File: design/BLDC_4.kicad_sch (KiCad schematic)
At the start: 39 parts, among them J1 Conn_01x03, J2 Conn_01x02, J3 Conn_02x06_Odd_Even, J6 Conn_02x06_Odd_Even, K1 SERVO, P101 CANBUS, P3 PWR_COMM, U8 MAX485ED, X1 MINI-USB-SHIELD-32005-201

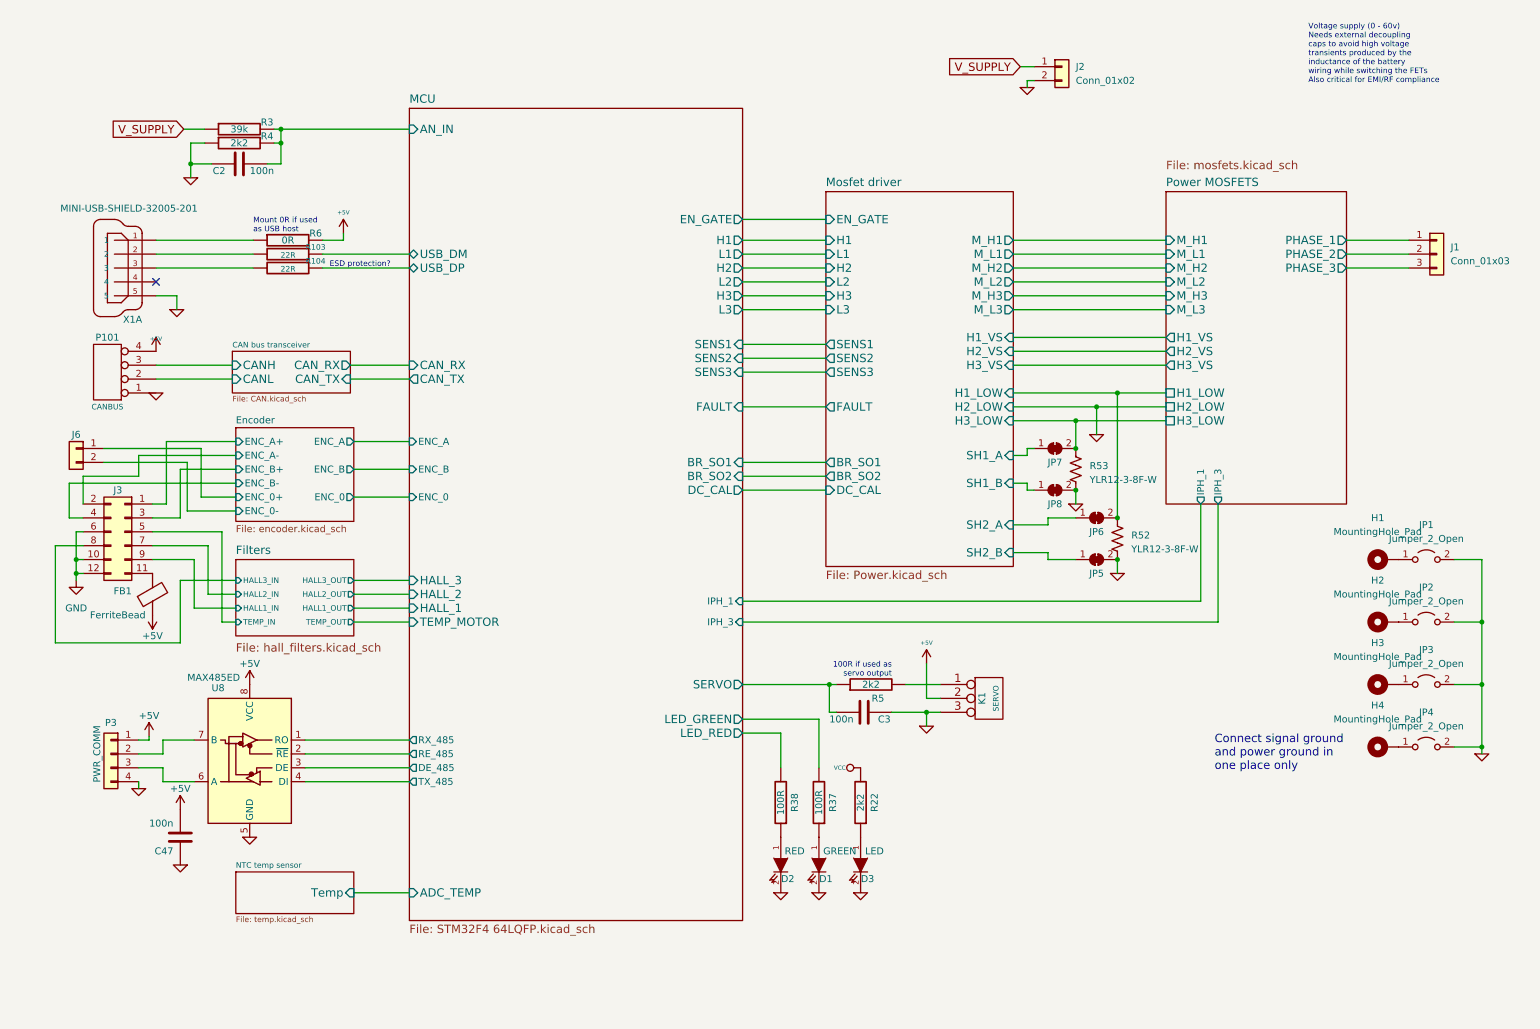
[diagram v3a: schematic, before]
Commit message: Changing to USB-C connector
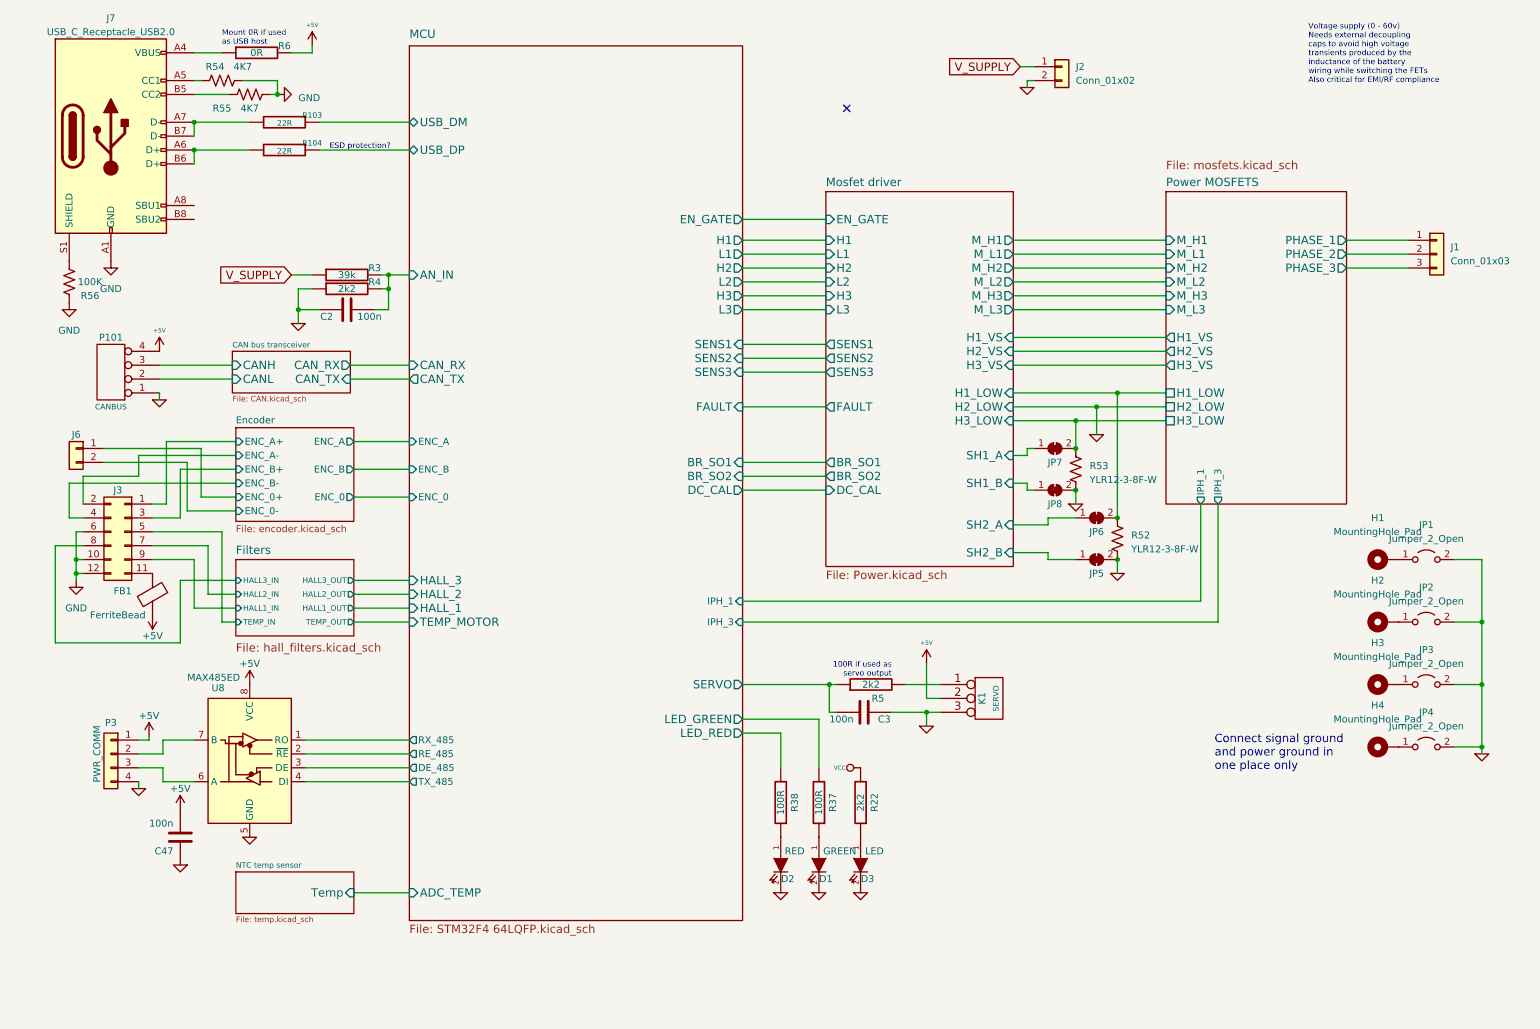
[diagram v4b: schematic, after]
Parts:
- removed X1: MINI-USB-SHIELD-32005-201, CRF1:USB-UX60R-MB-5ST, symbol BLDC_4-rescue:MINI-USB-SCHIELD-32005-201
- added J7: USB_C_Receptacle_USB2.0, Connector_USB:USB_C_Receptacle_G-Switch_GT-USB-7010ASV, symbol Connector:USB_C_Receptacle_USB2.0
- added R54, R55: 4K7, Resistor_SMD:R_0603_1608Metric_Pad0.98x0.95mm_HandSolder, symbol Device:R_US
- added R56: 100K, Resistor_SMD:R_0603_1608Metric_Pad0.98x0.95mm_HandSolder, symbol Device:R_US
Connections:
- net GND: now also J7.A1 (GND), J7.A12 (GND), J7.B1 (GND), J7.B12 (GND), R54.2, R55.2, R56.1
- net at R6.1: now also J7.A4 (VBUS), J7.A9 (VBUS), J7.B4 (VBUS), J7.B9 (VBUS)
- net at R103.2: now also J7.A7 (D-), J7.B7 (D-)
- net at R104.2: now also J7.A6 (D+), J7.B6 (D+)
- new net: J7.B5 (CC2), R55.1
- new net: J7.A5 (CC1), R54.1
- new net: J7.S1 (SHIELD), R56.2
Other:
- moved on the sheet: C2, P101, R103, R104, R3, R4, R6
